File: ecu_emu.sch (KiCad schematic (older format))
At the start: 29 parts, among them J1 Conn_02x06_Odd_Even, J2 Conn_01x04_Male, Q1 IRF7201PBF, U1 LD1117S33TR_SOT223, U2 STM32F105RBTx, U3 FAN73711, U4 E-L9637D, Y1 Crystal KX-9A

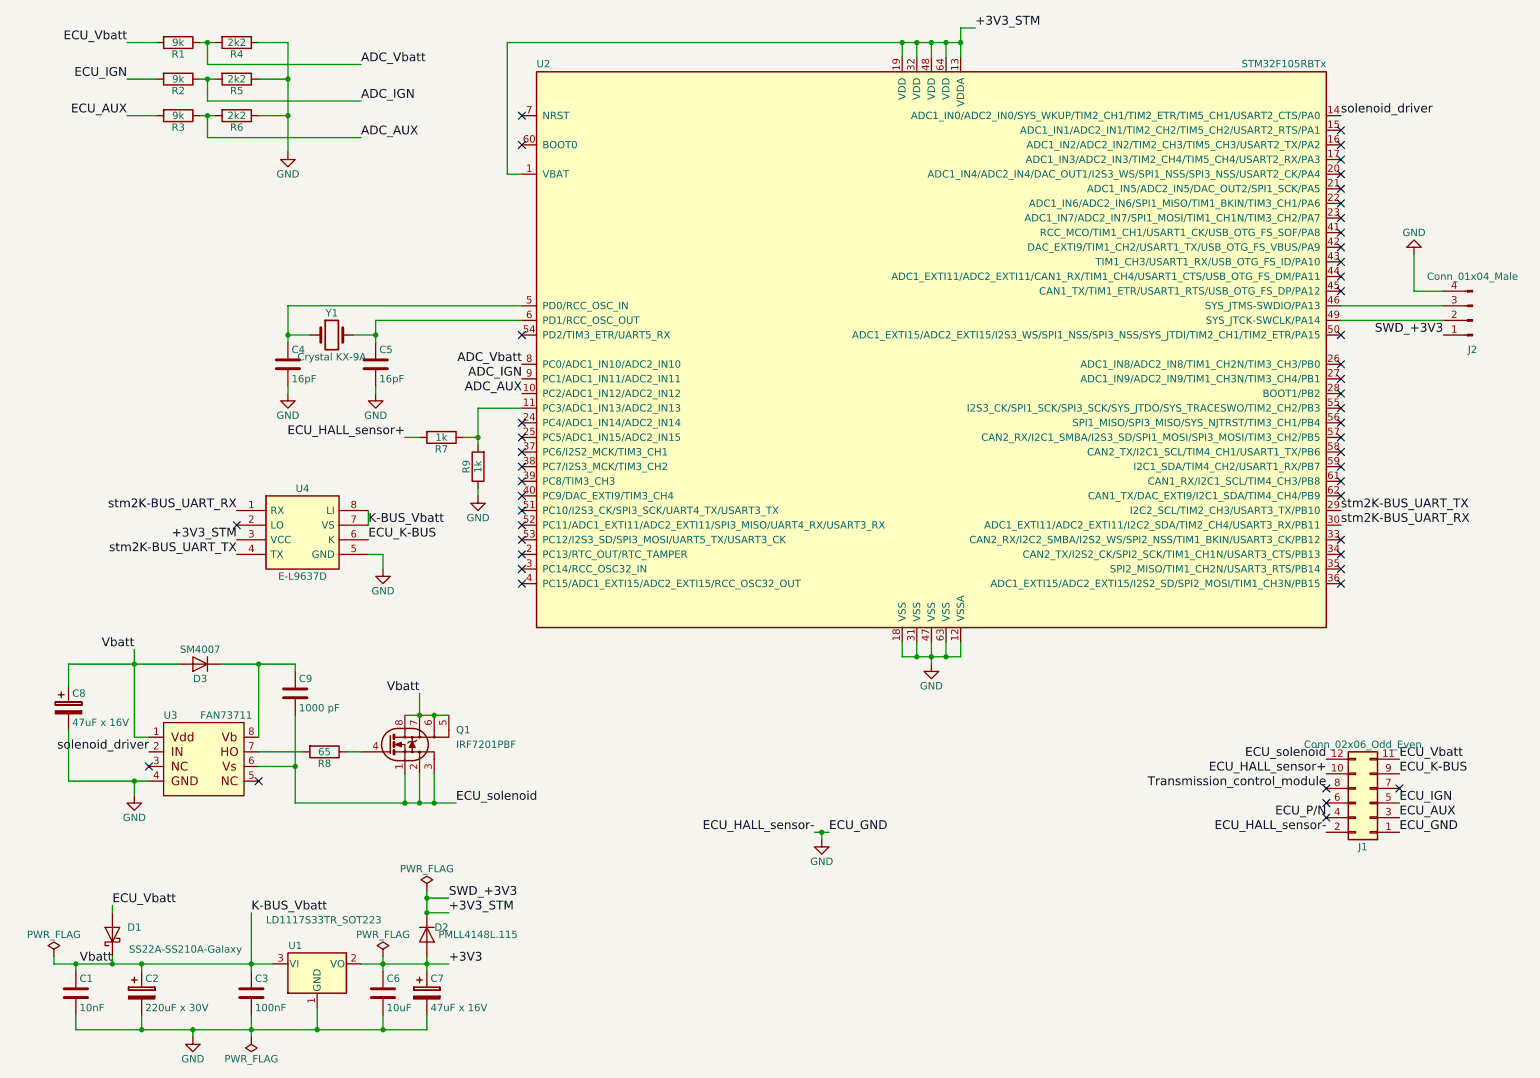
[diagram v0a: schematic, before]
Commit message: scheme: change solenoid driver, add capasitors to stm power supply, fix crystal package
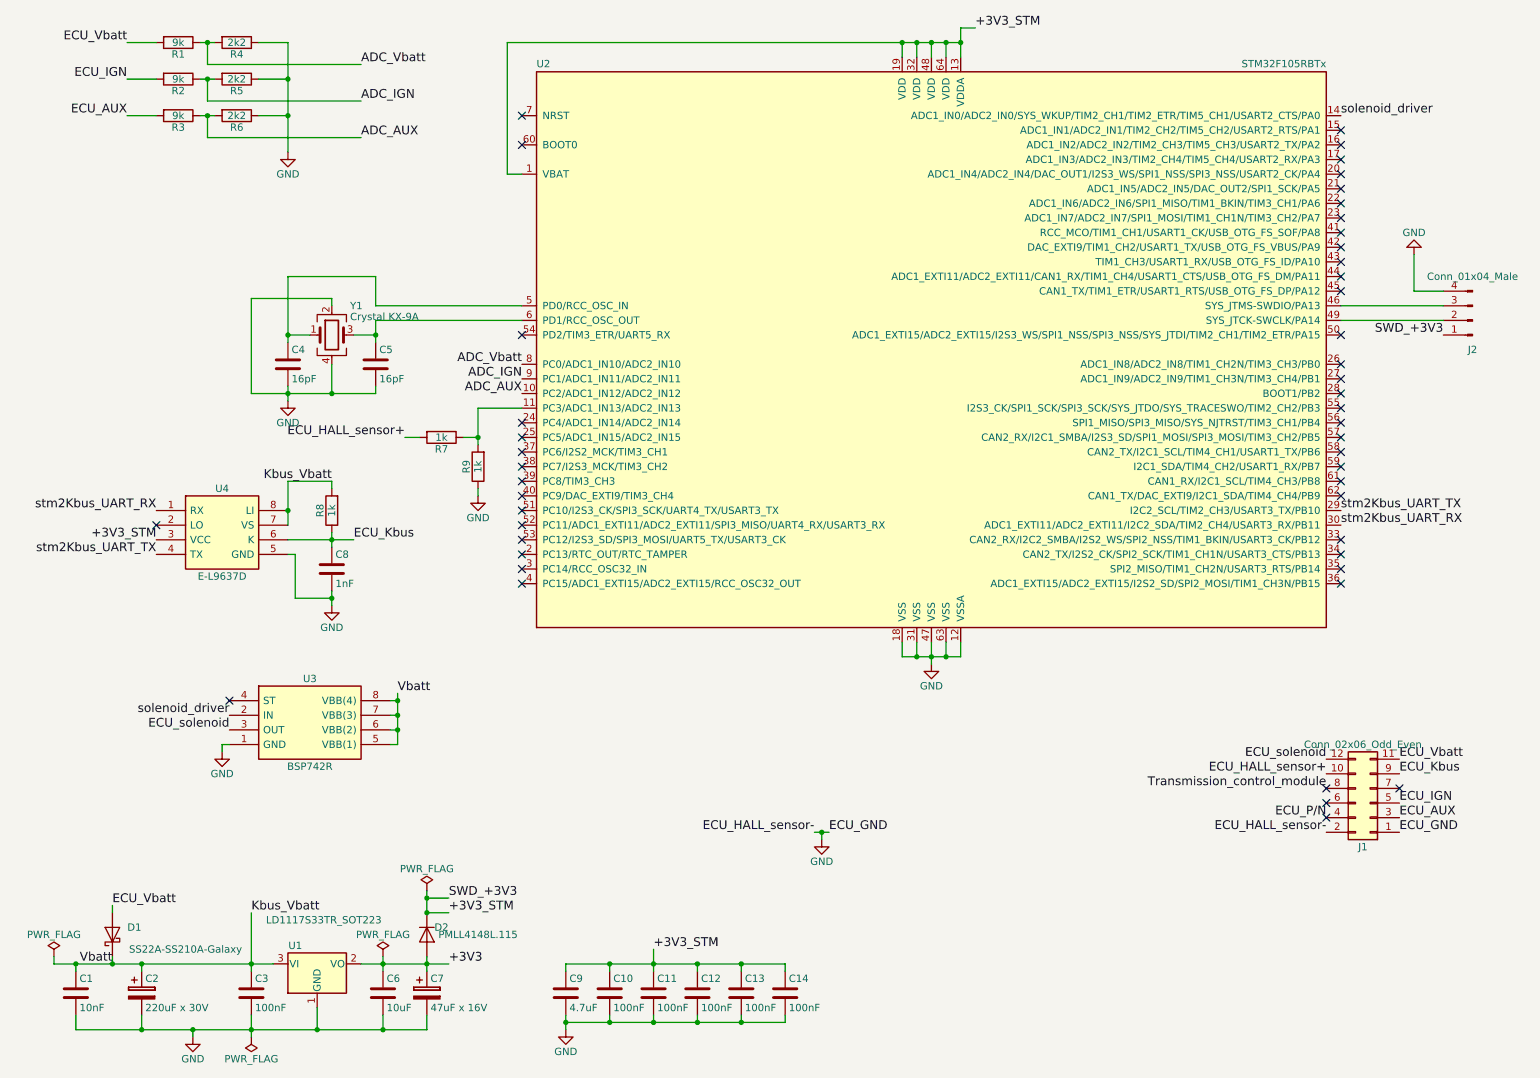
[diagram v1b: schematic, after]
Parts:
- removed C8: 47uF x 16V, Capacitors_Tantalum_SMD:CP_Tantalum_Case-C_EIA-6032-28_Wave, symbol CP
- removed D3: SM4007, Diodes_SMD:D_MELF, symbol D
- removed Q1: IRF7201PBF, Housings_SOIC:SOIC-8_3.9x4.9mm_Pitch1.27mm, symbol IRF7201PBF
- removed U3: FAN73711, Housings_SOIC:SOIC-8_3.9x4.9mm_Pitch1.27mm, symbol FAN73711
- removed Y1: Crystal KX-9A, Crystals:Crystal_SMD_5032-4pin_5.0x3.2mm, symbol Crystal
- added C10, C11, C12, C13, C14: 100nF, Capacitors_SMD:C_0805, symbol C
- added C8: 1nF, Capacitors_SMD:C_0805, symbol C
- added U3: BSP742R, zulljon:SOIC127P600X175-8N, symbol BSP742R
- added Y1: Crystal KX-9A, Crystals:Crystal_SMD_5032-4pin_5.0x3.2mm, symbol Crystal_GND24
- C9: value 1000 pF -> 4.7uF
- R8: value 65 -> 1k
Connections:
- net ECU_K-BUS is gone; now on net ECU_Kbus: J1.9 (Pin_9), U4.6 (K)
- net K-BUS_Vbatt is gone; now on net Kbus_Vbatt: C1.1, C2.1, C3.1, D1.1 (K), U1.3 (VI), U4.7 (VS), U4.8 (LI)
- net +3V3_STM: now also C9.1, C10.1, C11.1, C12.1, C13.1, C14.1
- net ECU_solenoid: now also U3.3 (OUT); no longer C9.2
- net GND: now also C9.2, C10.2, C11.2, C12.2, C13.2, C14.2, C8.2, U3.1 (GND), Y1.2, Y1.4
- net solenoid_driver: now also U3.2 (IN)
- net at C4.1, U2.5 (PD0/RCC_OSC_IN): now also Y1.1
- net at C5.1, U2.6 (PD1/RCC_OSC_OUT): now also Y1.3
- net ECU_Kbus: now reaches R8.1
- net ECU_Kbus: now also C8.1
- net Kbus_Vbatt: now reaches R8.2
- net Kbus_Vbatt: now also U3.5 (VBB(1)), U3.6 (VBB(2)), U3.7 (VBB(3)), U3.8 (VBB(4))
- net stm2K-BUS_UART_RX renamed stm2Kbus_UART_RX
- net stm2K-BUS_UART_TX renamed stm2Kbus_UART_TX
- no-connect marks 49 -> 48
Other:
- moved on the sheet: U4

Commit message: pcb: swd conn to socket strip, applied sch changes from 059fb19
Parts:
- J2: footprint Pin_Headers:Pin_Header_Straight_1x04_Pitch2.54mm -> Socket_Strips:Socket_Strip_Angled_1x04_Pitch2.54mm
- U3: footprint zulljon:SOIC127P600X175-8N -> Housings_SOIC:SOIC-8_3.9x4.9mm_Pitch1.27mm
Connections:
- net +3V3_STM: now also J2.4 (Pin_4); no longer J2.1 (Pin_1)
- net GND: now also J2.1 (Pin_1); no longer J2.4 (Pin_4)
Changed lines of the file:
@@
 F 0 "J2" H 10450 2850 50  0000 C CNN
 F 1 "Conn_01x04_Male" H 10450 2350 50  0000 C CNN
-F 2 "Pin_Headers:Pin_Header_Straight_1x04_Pitch2.54mm" H 10450 2650 50  0001 C CNN
+F 2 "Socket_Strips:Socket_Strip_Angled_1x04_Pitch2.54mm" H 10450 2650 50  0001 C CNN
 F 3 "" H 10450 2650 50  0001 C CNN
 	1    10450 2650
 	-1   0    0    1
 $EndComp
-Text Label 10250 2750 2    60   ~ 0
+Text Label 10250 2450 2    60   ~ 0
 SWD_+3V3
 Text Label 3450 6600 0    60   ~ 0
@@
 L GND #PWR09
 U 1 1 59EED690
-P 10050 2200
-F 0 "#PWR09" H 10050 1950 50  0001 C CNN
-F 1 "GND" H 10050 2050 50  0000 C CNN
-F 2 "" H 10050 2200 50  0001 C CNN
-F 3 "" H 10050 2200 50  0001 C CNN
-	1    10050 2200
-	-1   0    0    1
+P 10200 2800
+F 0 "#PWR09" H 10200 2550 50  0001 C CNN
+F 1 "GND" H 10200 2650 50  0000 C CNN
+F 2 "" H 10200 2800 50  0001 C CNN
+F 3 "" H 10200 2800 50  0001 C CNN
+	1    10200 2800
+	1    0    0    -1
 $EndComp
 Text Label 5950 6150 2    60   ~ 0
@@
 	750  7000 750  7050
 Connection ~ 1150 7050
-Wire Wire Line
-	10050 2200 10050 2450
-Wire Wire Line
-	10050 2450 10250 2450
 Connection ~ 6000 6150
 Wire Wire Line
@@
 F 0 "U3" H 2500 5400 50  0000 C CNN
 F 1 "BSP742R" H 2500 4800 50  0000 C CNN
-F 2 "zulljon:SOIC127P600X175-8N" H 2500 4700 50  0001 C CNN
+F 2 "Housings_SOIC:SOIC-8_3.9x4.9mm_Pitch1.27mm" H 2500 4700 50  0001 C CNN
 F 3 "http://docs-europe.electrocomponents.com/webdocs/1074/0900766b8107439c.pdf" H 2500 4600 50  0001 C CNN
 F 4 "Smart High-Side Power Switch 34V DSO-8 ISP742RI, Intelligent Power Switch High Side Switch, 0.4A, -10 ??? 16V, 8-Pin, PG-DSO-8-24" H 2500 4500 50  0001 C CNN "Description"
@@
 $EndComp
 NoConn ~ 1950 5250
+Wire Wire Line
+	10250 2750 10200 2750
+Wire Wire Line
+	10200 2750 10200 2800
 $EndSCHEMATC

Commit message: sch&pcb: add one LED and refresh readme image
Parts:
- added D3: LED, LEDs:LED_0805, symbol LED
- added R10: 1k, Resistors_SMD:R_0805, symbol R
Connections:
- net GND: now also D3.1 (K)
- net at U2.26 (ADC1_IN8/ADC2_IN8/TIM1_CH2N/TIM3_CH3/PB0): now also R10.2
- new net: D3.2 (A), R10.1
- no-connect marks 48 -> 47
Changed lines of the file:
@@
 NoConn ~ 9550 3150
 NoConn ~ 9550 3050
-NoConn ~ 9550 2950
 NoConn ~ 9550 2750
 NoConn ~ 9550 2450
@@
 $EndComp
 Wire Wire Line
-	4250 7500 4250 7400
-Wire Wire Line
-	5750 7400 5750 7450
-Wire Wire Line
-	5750 7450 4250 7450
+	4250 7400 4250 7500
+Wire Wire Line
+	5750 7450 5750 7400
+Wire Wire Line
+	4250 7450 5750 7450
 Connection ~ 4250 7450
 Wire Wire Line
@@
 Connection ~ 5450 7450
 Wire Wire Line
-	5750 7100 5750 7050
-Wire Wire Line
-	5750 7050 4250 7050
+	5750 7050 5750 7100
+Wire Wire Line
+	4250 7050 5750 7050
 Wire Wire Line
 	4250 7050 4250 7100
@@
 Wire Wire Line
 	10200 2750 10200 2800
+$Comp
+L R R10
+U 1 1 5A257B4D
+P 9900 3150
+F 0 "R10" V 9980 3150 50  0000 C CNN
+F 1 "1k" V 9900 3150 50  0000 C CNN
+F 2 "Resistors_SMD:R_0805" V 9830 3150 50  0001 C CNN
+F 3 "" H 9900 3150 50  0001 C CNN
+	1    9900 3150
+	0    1    1    0
+$EndComp
+Wire Wire Line
+	9550 2950 9700 2950
+Wire Wire Line
+	9700 2950 9700 3150
+Wire Wire Line
+	9700 3150 9750 3150
+Wire Wire Line
+	10050 3150 10200 3150
+$Comp
+L GND #PWR015
+U 1 1 5A257E23
+P 10650 3200
+F 0 "#PWR015" H 10650 2950 50  0001 C CNN
+F 1 "GND" H 10650 3050 50  0000 C CNN
+F 2 "" H 10650 3200 50  0001 C CNN
+F 3 "" H 10650 3200 50  0001 C CNN
+	1    10650 3200
+	1    0    0    -1
+$EndComp
+Wire Wire Line
+	10650 3200 10650 3150
+Wire Wire Line
+	10650 3150 10500 3150
+$Comp
+L LED D3
+U 1 1 5A257F36
+P 10350 3150
+F 0 "D3" H 10350 3250 50  0000 C CNN
+F 1 "LED" H 10350 3050 50  0000 C CNN
+F 2 "LEDs:LED_0805" H 10350 3150 50  0001 C CNN
+F 3 "" H 10350 3150 50  0001 C CNN
+	1    10350 3150
+	-1   0    0    1
+$EndComp
 $EndSCHEMATC

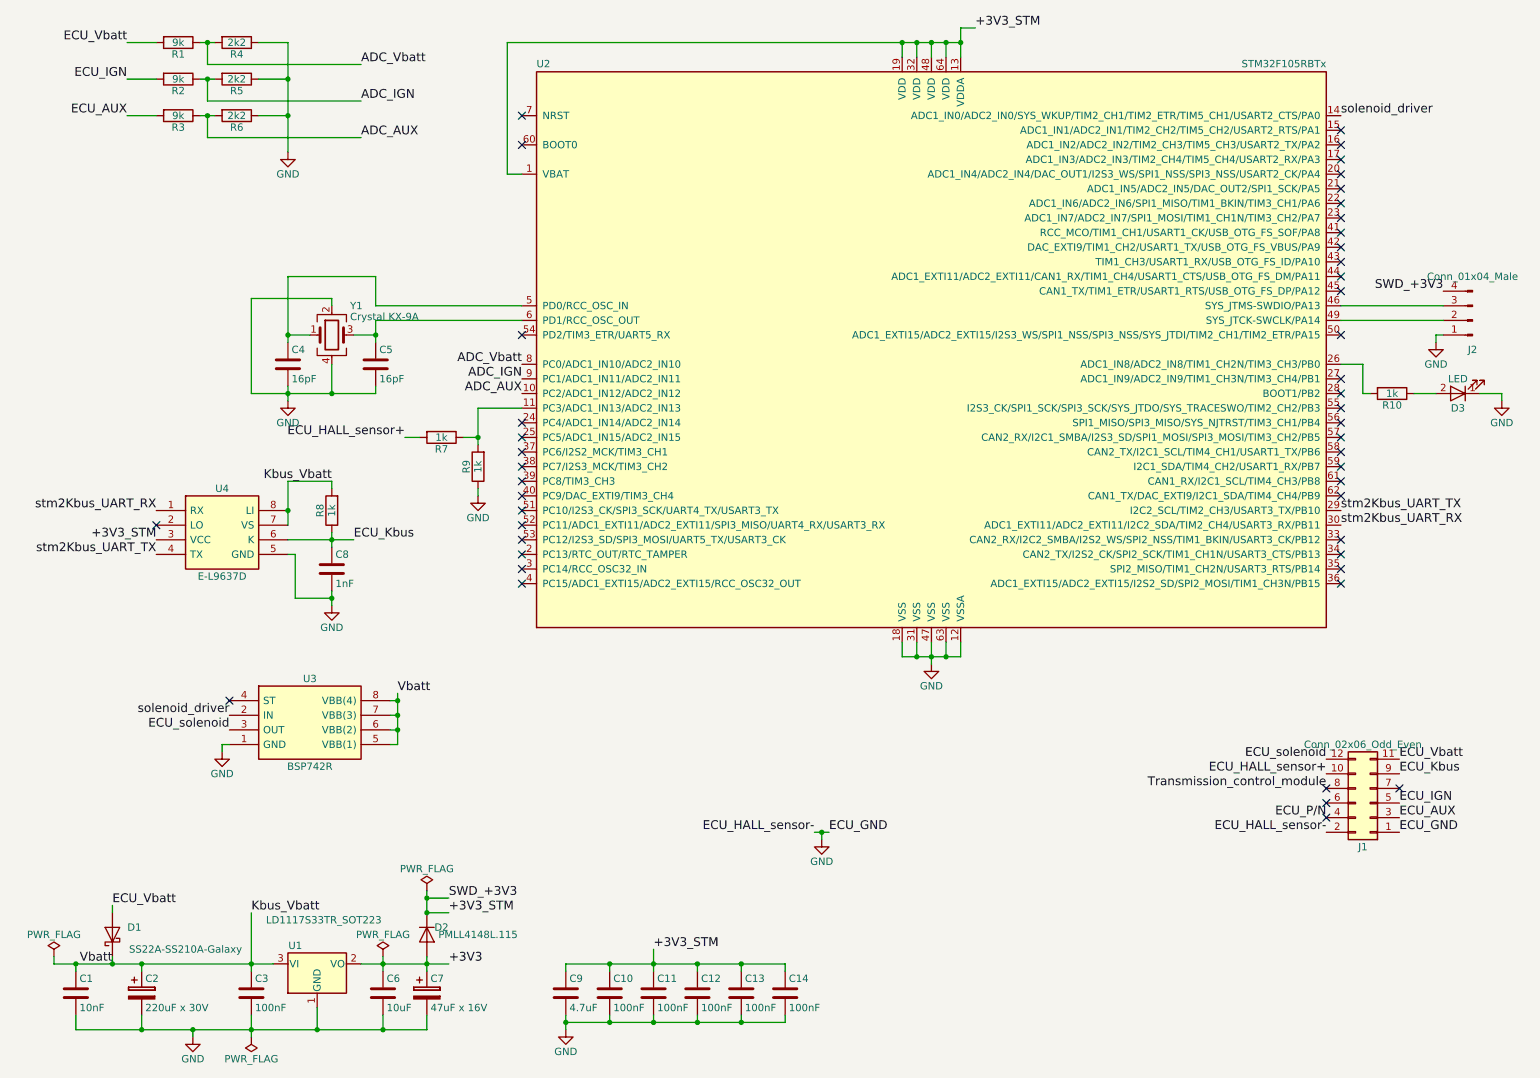
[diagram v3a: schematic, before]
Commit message: more fixes 1. separate power on k-bus IC logic 2. D2 change to shottky diod 3. pull-up on stm RESET pin 4. change linier stabilizer to adjastable version, to make apropriate voltage on stm throw diod
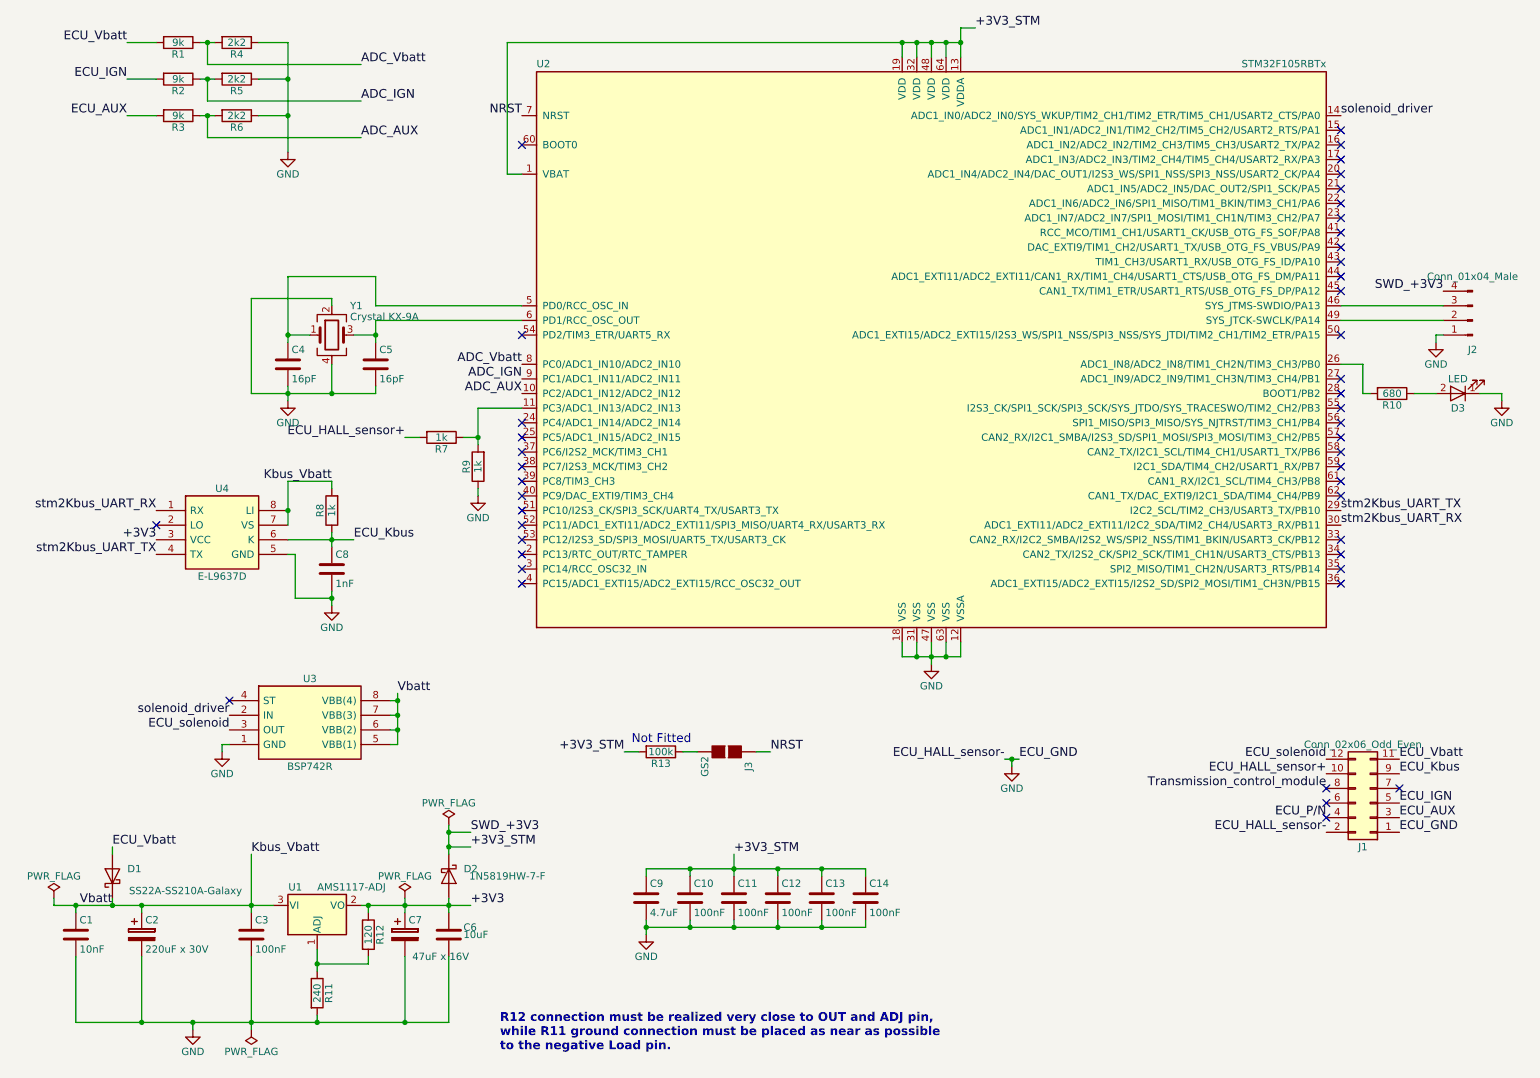
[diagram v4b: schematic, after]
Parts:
- removed D2: PMLL4148L.115, Diodes_SMD:D_SC-80, symbol D
- removed U1: LD1117S33TR_SOT223, TO_SOT_Packages_SMD:SOT-223-3_TabPin2, symbol LD1117S33TR_SOT223
- added D2: 1N5819HW-7-F, Diodes_SMD:D_SOD-123, symbol D_Schottky
- added J3: GS2, Connectors:GS2, symbol GS2
- added R11: 240, Resistors_SMD:R_0805, symbol R
- added R12: 120, Resistors_SMD:R_0805, symbol R
- added R13: 100k, Resistors_SMD:R_0805, symbol R
- added U1: AMS1117-ADJ, TO_SOT_Packages_SMD:SOT-223-3_TabPin2, symbol LM1117-ADJ
- R10: value 1k -> 680
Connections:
- net +3V3: now also U4.3 (VCC), D2.2 (A), R12.1, U1.2 (VO)
- net +3V3_STM: now also D2.1 (K), R13.2; no longer U4.3 (VCC)
- net GND: now also R11.2
- net Kbus_Vbatt: now also U1.3 (VI)
- net NRST: now reaches U2.7 (NRST)
- net NRST: now also J3.1 (G1)
- new net: R11.1, R12.2, U1.1 (ADJ)
- new net: J3.2 (G2), R13.1
- no-connect marks 47 -> 46
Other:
- note added: "Not Fitted"
- note added: "R12 connection must be realized very close to OUT and ADJ pin,\nwhile R11 ground connection must be placed as near as possible\nto the negative Load pin."
- moved on the sheet: C1, C10, C11, C12, C13, C14, C2, C3, C6, C7, C9, D1
